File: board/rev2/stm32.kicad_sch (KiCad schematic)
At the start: 6 parts, among them J3 Conn_01x03, U6 STM32G071CBUx

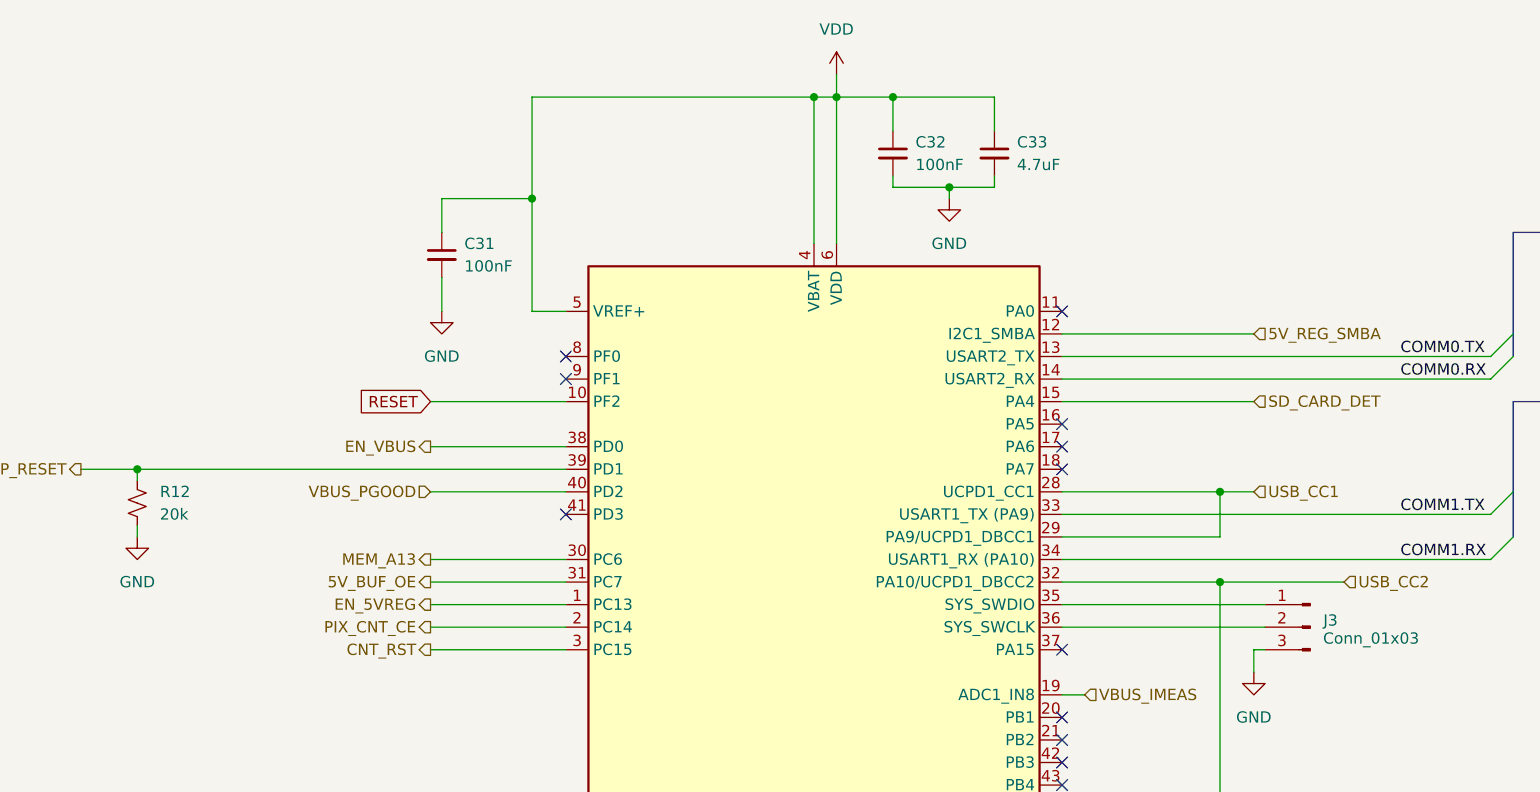
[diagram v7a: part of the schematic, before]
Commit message: Really finish rev2 board schematic
- fix some more footprints
  - move to real SD card holder, for example
- repair part numbers
- add LCSC part refs to everything
- add even more caps to the 3.3V reg output
  - really should use an LDO but meh it should be fine

total BOM cost for 5 of them is apparently 160 CAD, or like 32 dollars
each (don't think that includes the feeder fees tho)
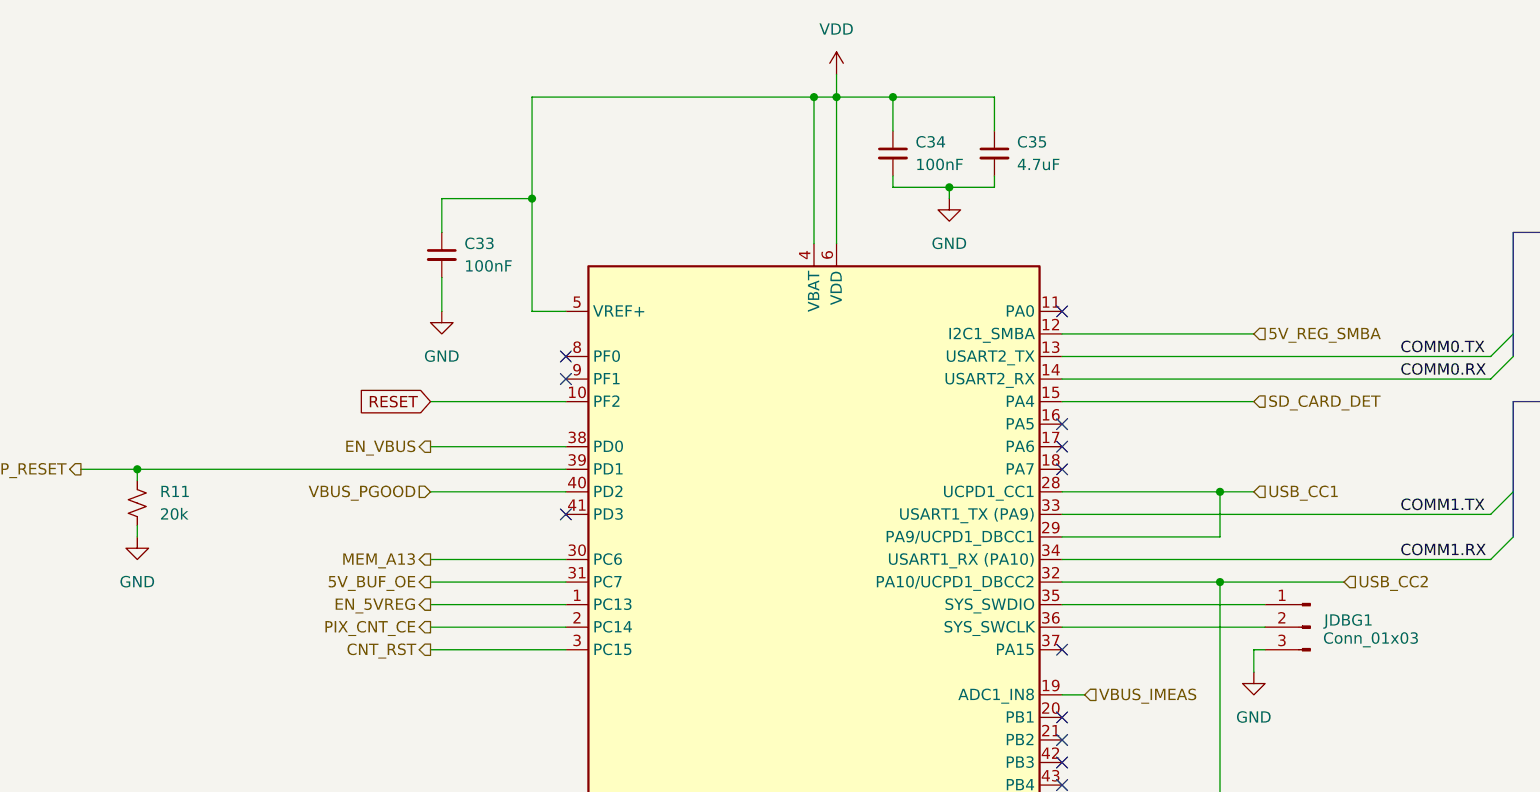
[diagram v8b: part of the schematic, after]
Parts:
- C33: renamed from C31; LCSC (none) -> C307331
- C34: renamed from C32; LCSC (none) -> C307331
- C35: renamed from C33; LCSC (none) -> C29823
- R11: renamed from R12; LCSC (none) -> C4184
- U6: LCSC (none) -> C529343; Part STM32G071CBUx -> STM32G071CBU6
- renumbered J3 to JDBG1
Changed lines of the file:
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@@
 		(dnp no)
 		(fields_autoplaced yes)
-		(property "Reference" "C31"
+		(property "Reference" "C33"
 			(at 91.44 49.5362 0)
 			(effects
@@
 			)
 		)
+		(property "LCSC" "C307331 "
+			(at 88.9 50.8 0)
+			(effects
+				(font
+					(size 1.27 1.27)
+				)
+				(hide yes)
+			)
+		)
 		(pin "1"
 		)
@@
 			(project ""
 				(path "/32eb05c7-b4a6-42f3-8fb3-43453631100f/4f7f35d0-2952-4294-913c-05f668985375"
-					(reference "C31")
+					(reference "C33")
 					(unit 1)
 				)
@@
 		(dnp no)
 		(fields_autoplaced yes)
-		(property "Reference" "C33"
+		(property "Reference" "C35"
 			(at 153.67 38.1062 0)
 			(effects
@@
 			)
 		)
+		(property "LCSC" "C29823 "
+			(at 151.13 39.37 0)
+			(effects
+				(font
+					(size 1.27 1.27)
+				)
+				(hide yes)
+			)
+		)
 		(pin "1"
 		)
@@
 			(project ""
 				(path "/32eb05c7-b4a6-42f3-8fb3-43453631100f/4f7f35d0-2952-4294-913c-05f668985375"
-					(reference "C33")
+					(reference "C35")
 					(unit 1)
 				)
@@
 		(dnp no)
 		(fields_autoplaced yes)
-		(property "Reference" "R12"
+		(property "Reference" "R11"
 			(at 57.15 77.4699 0)
 			(effects
@@
 			)
 		)
+		(property "LCSC" "C4184"
+			(at 54.61 78.74 0)
+			(effects
+				(font
+					(size 1.27 1.27)
+				)
+				(hide yes)
+			)
+		)
 		(pin "2"
 		)
@@
 			(project ""
 				(path "/32eb05c7-b4a6-42f3-8fb3-43453631100f/4f7f35d0-2952-4294-913c-05f668985375"
-					(reference "R12")
+					(reference "R11")
 					(unit 1)
 				)
@@
 		(on_board yes)
 		(dnp no)
-		(property "Reference" "J3"
-			(at 188.976 91.948 0)
+		(property "Reference" "JDBG1"
+			(at 191.008 91.948 0)
 			(effects
 				(font
@@
 			)
 		)
+		(property "LCSC" ""
+			(at 186.69 92.71 0)
+			(effects
+				(font
+					(size 1.27 1.27)
+				)
+				(hide yes)
+			)
+		)
 		(pin "2"
 		)
@@
 			(project "mainboard"
 				(path "/32eb05c7-b4a6-42f3-8fb3-43453631100f/4f7f35d0-2952-4294-913c-05f668985375"
-					(reference "J3")
+					(reference "JDBG1")
 					(unit 1)
 				)
@@
 		(dnp no)
 		(fields_autoplaced yes)
-		(property "Reference" "C32"
+		(property "Reference" "C34"
 			(at 142.24 38.1062 0)
 			(effects
@@
 			)
 		)
+		(property "LCSC" "C307331 "
+			(at 139.7 39.37 0)
+			(effects
+				(font
+					(size 1.27 1.27)
+				)
+				(hide yes)
+			)
+		)
 		(pin "1"
 		)
@@
 			(project ""
 				(path "/32eb05c7-b4a6-42f3-8fb3-43453631100f/4f7f35d0-2952-4294-913c-05f668985375"
-					(reference "C32")
+					(reference "C34")
 					(unit 1)
 				)
@@
 			)
 		)
-		(property "Part" "STM32G071CBUx"
+		(property "Part" "STM32G071CBU6"
 			(at 130.81 97.79 0)
 			(effects
+				(font
+					(size 1.27 1.27)
+				)
+				(hide yes)
+			)
+		)
+		(property "LCSC" "C529343"
+			(at 130.81 97.79 0)
+			(effects
